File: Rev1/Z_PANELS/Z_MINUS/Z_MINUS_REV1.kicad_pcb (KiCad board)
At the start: 2 copper layers, 98 x 98 mm, 54 parts, among them IC1 LTC4316IDD#PBF, IC2 SM141K08TFV, IC3 SM141K04TFV, IC4 SM141K04TFV, IC5 SM141K04TFV, IC6 SM141K08TFV, Q1 BSS138, Q2 BSS138, Q3 MBT2222ADW1T1, Q4 BSS138, Q5 BSS138, Q6 MBT2222ADW1T1, U1 OPT4001DTST, U2 LTC3130EUDC-1-PBF

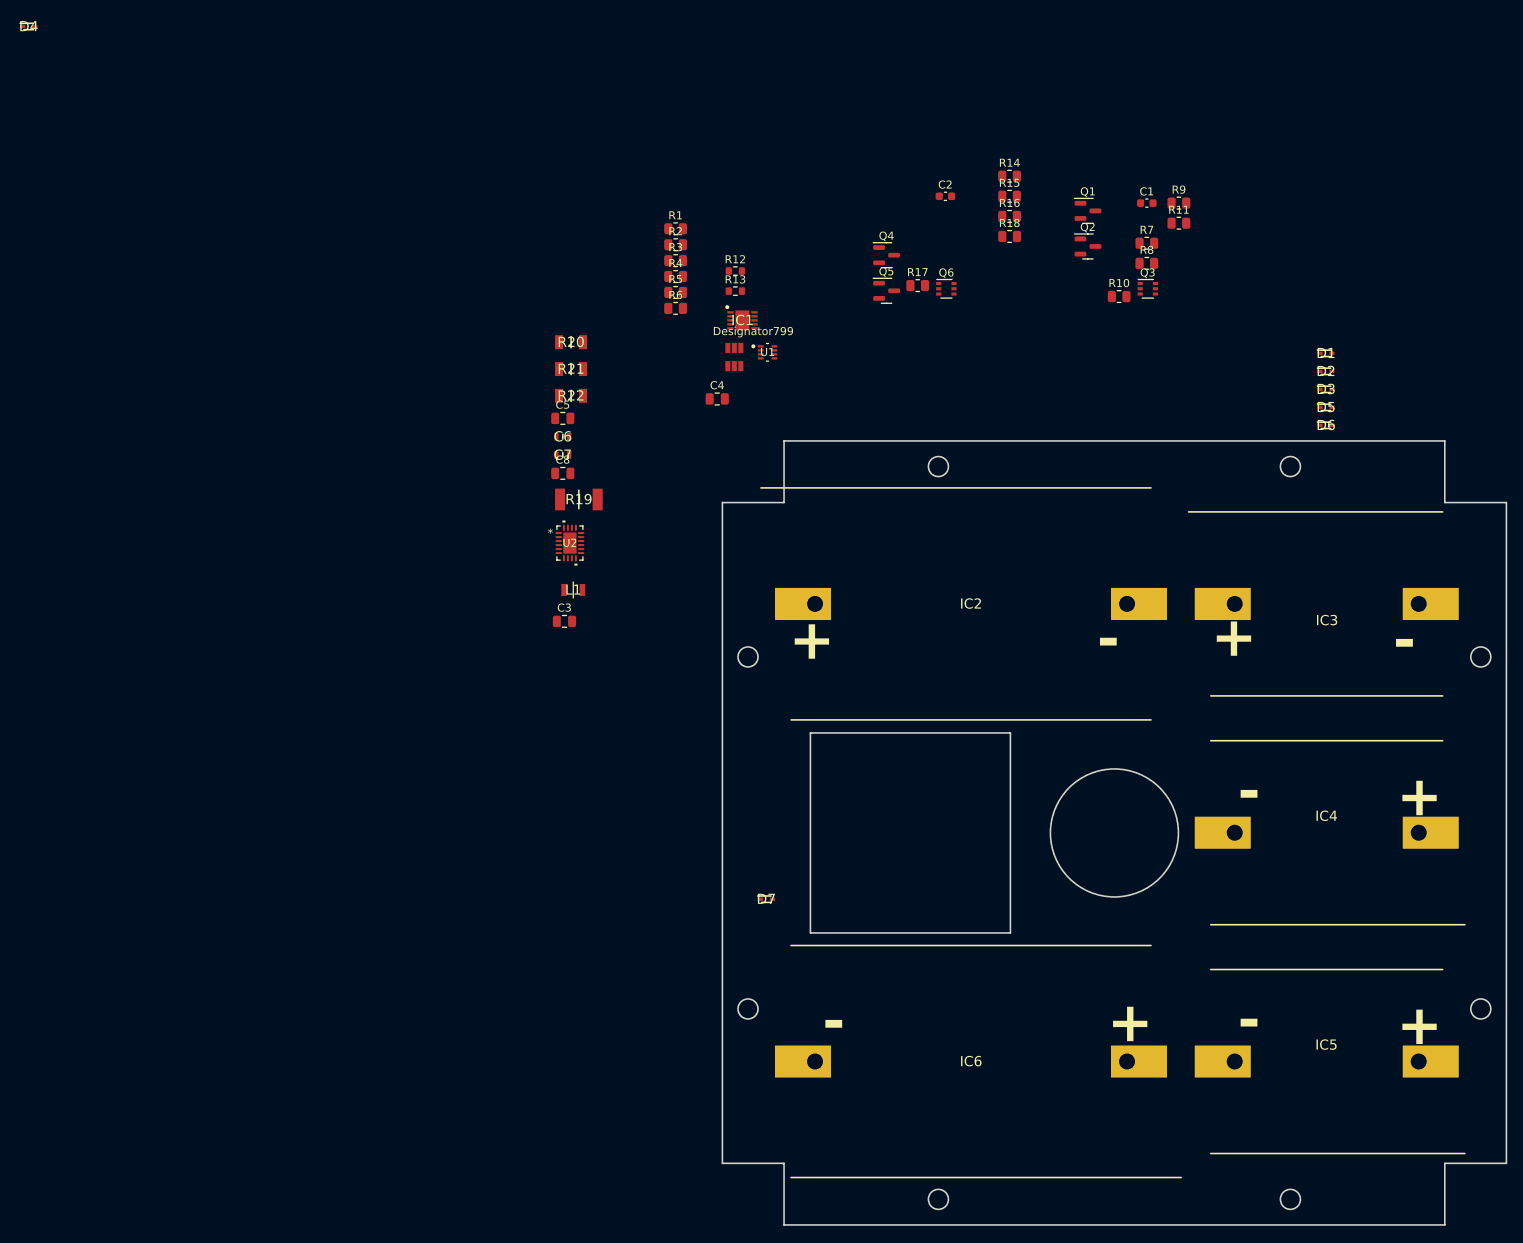
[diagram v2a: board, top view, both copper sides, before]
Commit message: finished Z minus board design
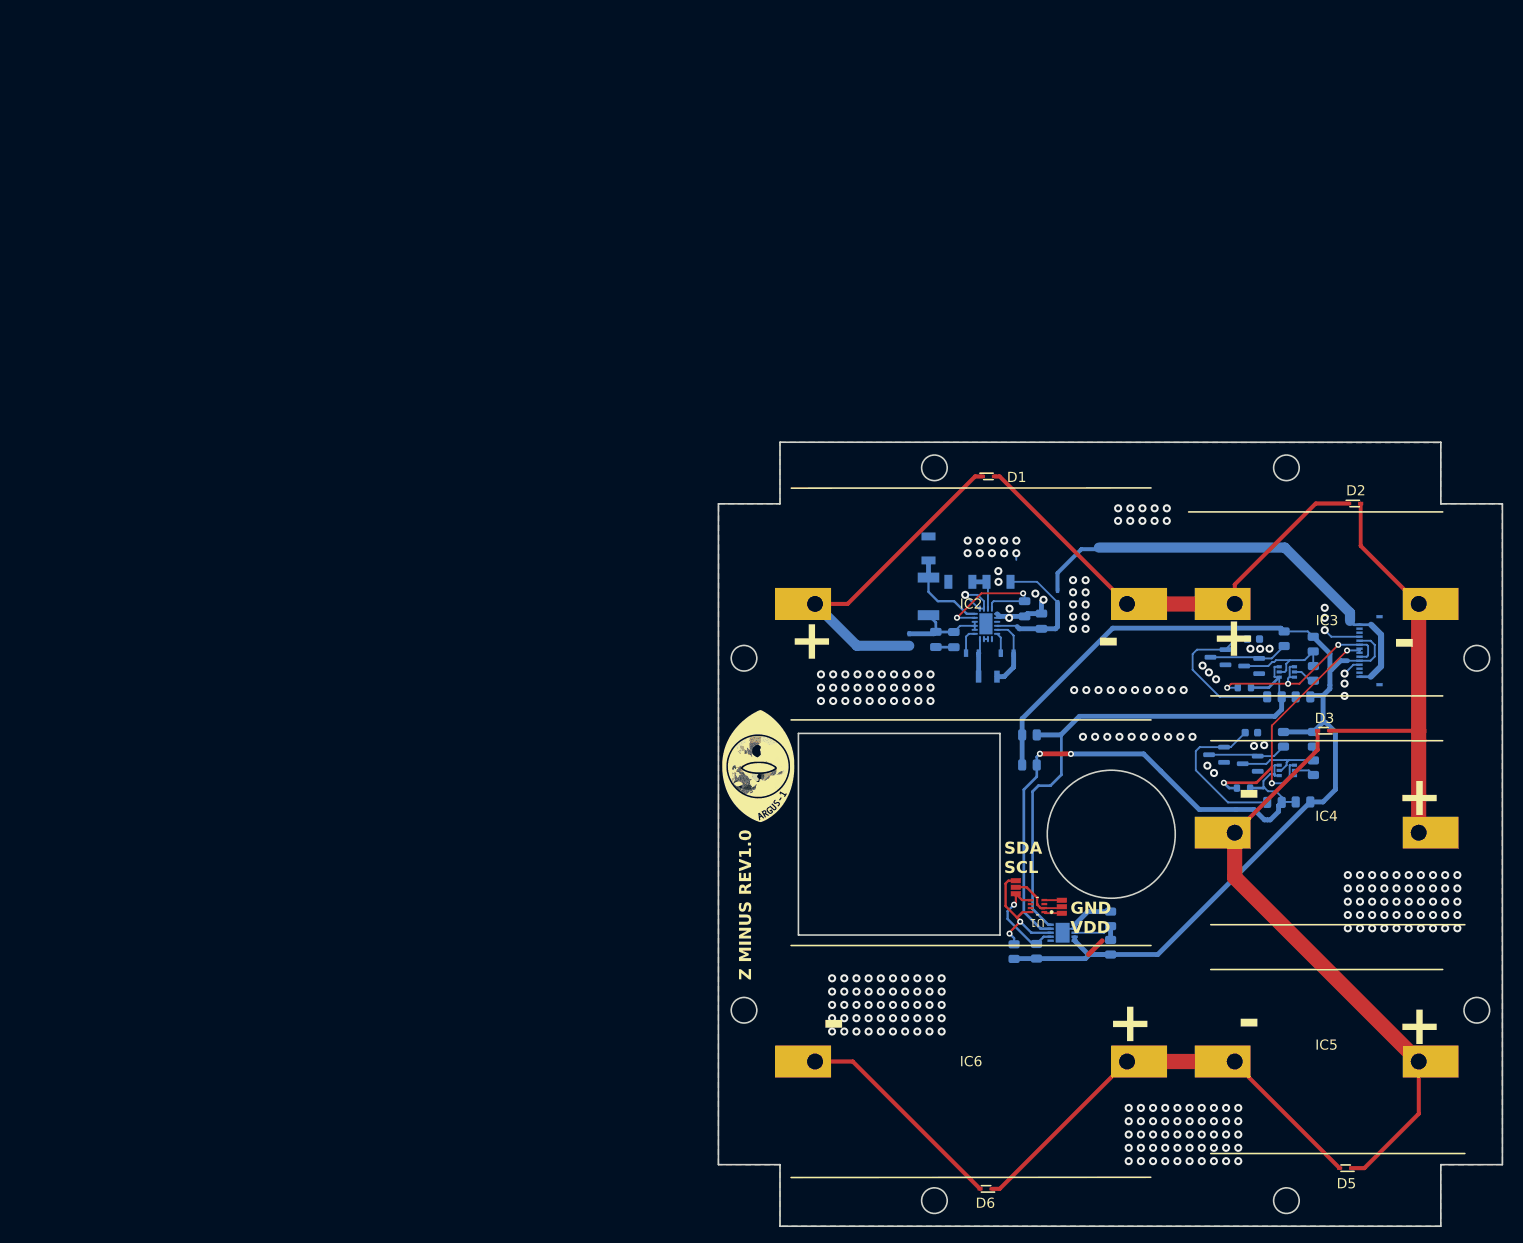
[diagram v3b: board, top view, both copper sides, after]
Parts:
- added .: ., argus:Argus LOGO, F.Cu at (92.4, 93.3)
- added .: ., argus:Argus LOGO, B.Cu at (169.9, 120.3)
- added J1: F3311A7H121014E200, AA_AUTO_LOADER:F3311A7H121014E200, B.Cu at (168.9, 78.7)
- C1, C2, C3, C4, C5, C6, C7, C8, D4, D7, IC1, L1, Q1, Q2, Q3, Q4, Q5, Q6, R1, R10, R11, R12, R13, R14, R15, R16, R17, R18, R19, R2, R20, R21, R22, R3, R4, R5, R6, R7, R8, R9, U2: moved to B.Cu
- moved D4 134.1 mm to (111.3, 77.3), turned to -90 degrees
- moved D6 104.5 mm to (120.9, 145.9), turned to 180 degrees
- moved R2 103.3 mm to (136.5, 115.7), turned to 90 degrees
- moved R1 102.0 mm to (136.5, 112.2), turned to 90 degrees
- moved R3 97.4 mm to (127.2, 116.2), turned to -90 degrees
- moved D5 95.1 mm to (165.9, 143.3), turned to 180 degrees
- moved R4 94.4 mm to (124.4, 116.3), turned to -90 degrees
- moved R13 88.8 mm to (153.1, 95.8)
- moved IC1 86.4 mm to (130.5, 113.9), turned to 180 degrees
- moved R12 82.2 mm to (153.2, 83.3)
- moved R15 80.9 mm to (161.8, 93.3), turned to 90 degrees
- moved R17 80.5 mm to (160.5, 97.6)
- moved JP2 79.0 mm to (130.4, 110.6), turned to -90 degrees
- moved R14 78.3 mm to (158.1, 89.7), turned to 90 degrees
- moved Q4 78.1 mm to (153.9, 92.8), turned to 180 degrees
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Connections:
- D2 pad 2: unconnected-(D2-Pad2) -> Net-(IC3-NEG)
- Q1 pad 2: Net-(Q1-S) -> GND
- Q1 pad 3: GND -> Net-(Q1-D)
- Q2 pad 2: Net-(Q1-G) -> GND
- Q2 pad 3: GND -> Net-(Q1-G)
- Q3 pad 5: Net-(Q1-S) -> Net-(Q1-D)
- Q4 pad 2: Net-(Q4-S) -> GND
- Q4 pad 3: GND -> Net-(Q4-D)
- Q5 pad 2: Net-(Q4-G) -> GND
- Q5 pad 3: GND -> Net-(Q4-G)
- Q6 pad 5: Net-(Q4-S) -> Net-(Q4-D)
- R15 pad 2: Net-(Q4-S) -> Net-(Q4-D)
- R16 pad 2: Net-(Q4-S) -> Net-(Q4-D)
- R8 pad 1: Net-(Q1-S) -> Net-(Q1-D)
- R9 pad 2: Net-(Q1-S) -> Net-(Q1-D)
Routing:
- net +3.3V: track 0.00 -> 139.9 mm
- net SCL_SUN: track 0.00 -> 74.9 mm
- net Net-(IC4-NEG): track 0.00 -> 72.9 mm
- net SDA_SUN: track 0.00 -> 71.8 mm, vias 0 -> 2
- net GND: track 0.00 -> 64.5 mm, vias 0 -> 253
- net Net-(IC2-NEG): track 0.00 -> 57.5 mm
- net VSOLAR: track 0.00 -> 56.2 mm
- net Net-(IC5-NEG): track 0.00 -> 55.7 mm
- net Net-(IC3-NEG): track 0.00 -> 55.3 mm
- net /SOLAR_PANEL_ELECTRONICS/7023_vout: track 0.00 -> 41.5 mm
- net SDA1_b4iso: track 0.00 -> 36.4 mm, vias 0 -> 3
- net SCL1_b4iso: track 0.00 -> 26.9 mm, vias 0 -> 3
- net Net-(Q2-G): track 0.00 -> 20.3 mm
- net Net-(Q5-G): track 0.00 -> 20.1 mm
- net Net-(U2-VOUT): track 0.00 -> 17.8 mm
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- added copper zone on B.Cu, net GND
- added copper zone on F.Cu, net GND
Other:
- outline, holes or cut-outs redrawn
- rule pad_to_mask_clearance: 0 -> 0.0508
- board text added: "DNP"
- board text added: "GND VDD"
- board text added: "SDA SCL"
- board text added: "Z MINUS REV1.0"
- board text added: "Z MINUS REV1.0 DESIGNED BY NISCHAL FEB 24"

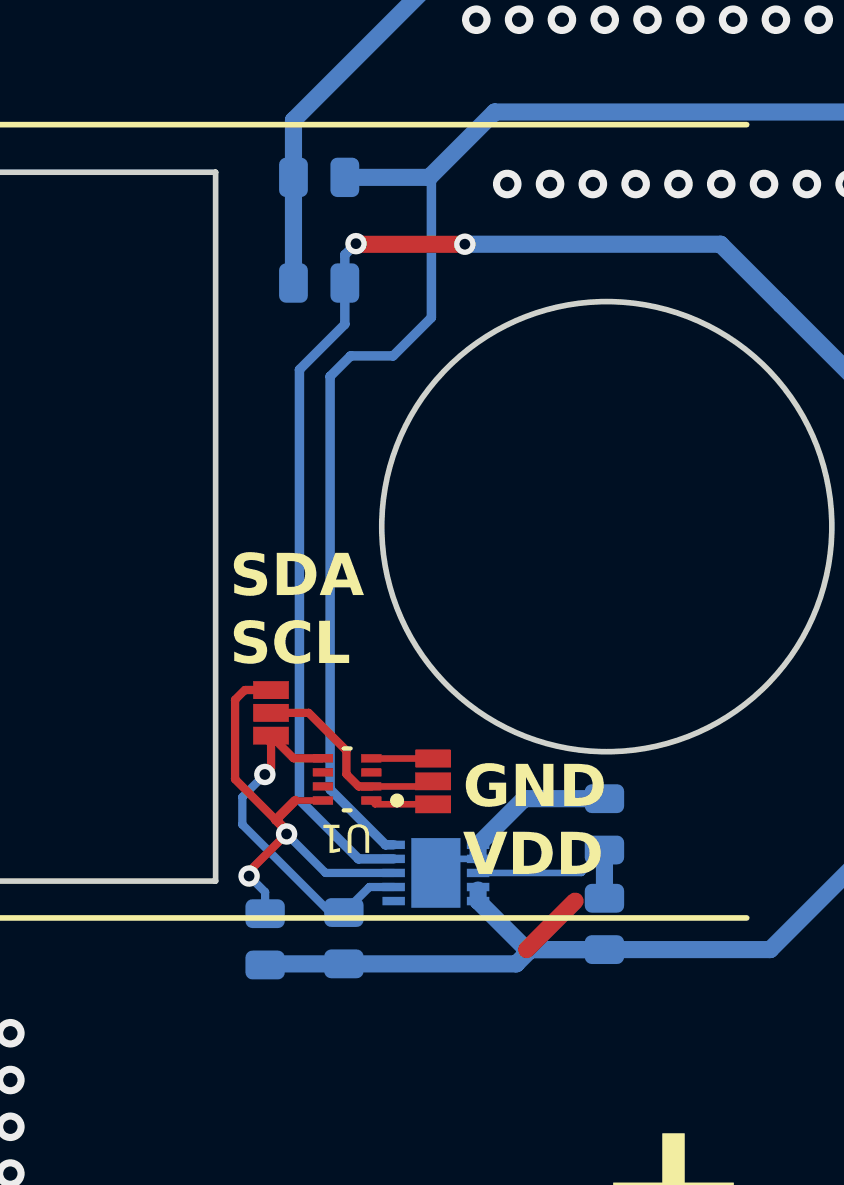
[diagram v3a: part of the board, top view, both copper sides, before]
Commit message: fixed bug in Z minus
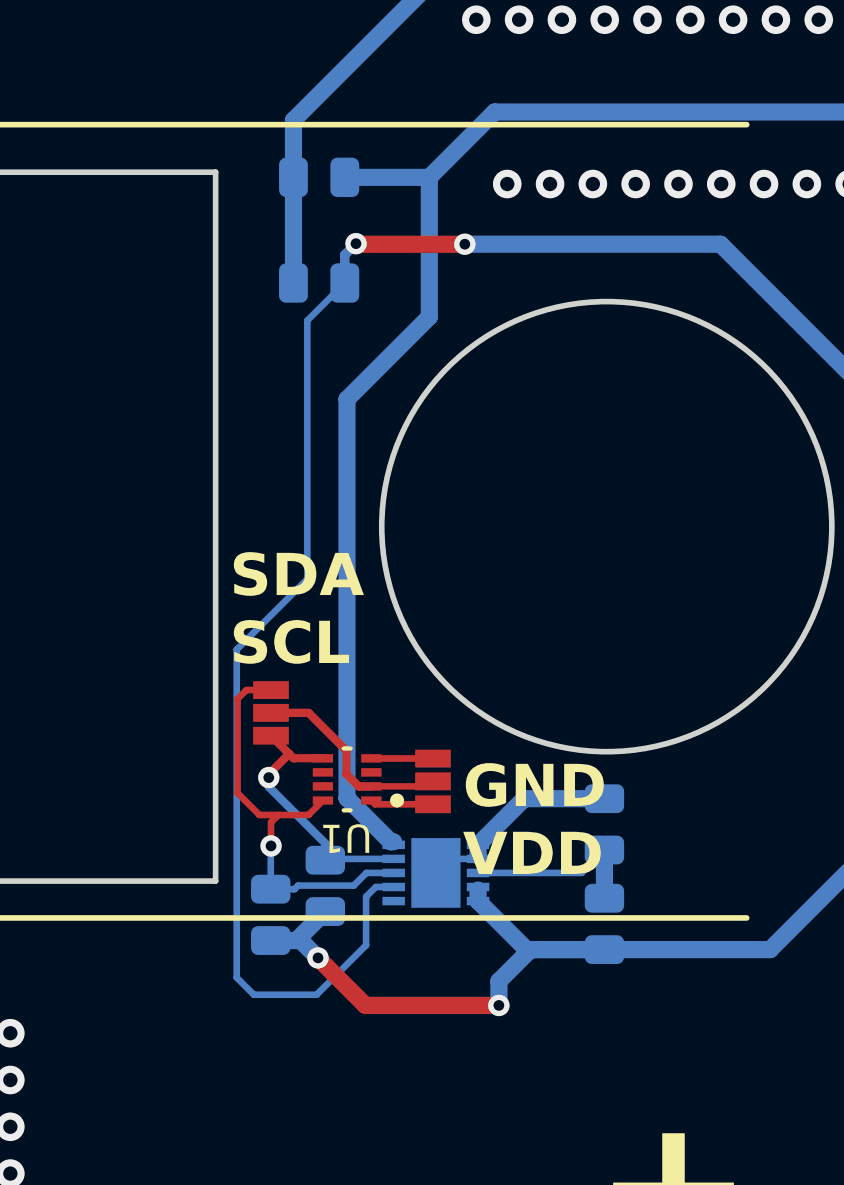
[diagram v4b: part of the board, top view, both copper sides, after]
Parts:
- moved R3 1.97 mm to (126.6, 114.4)
- moved R4 0.89 mm to (124.6, 115.4)
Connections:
- IC1 pad 7: SCL_4001 -> SDA_SUN
- IC1 pad 9: SDA_SUN -> SCL_4001
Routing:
- net SDA_SUN: track 71.8 -> 83.2 mm
- net SCL_SUN: track 74.9 -> 70.2 mm
- net +3.3V: track 139.9 -> 144.2 mm, vias 0 -> 2
- net SCL_4001: track 12.8 -> 9.54 mm
- net GND: track 64.5 -> 62.1 mm
- net SDA_4001: track 16.9 -> 15.6 mm, vias 2 -> 1
